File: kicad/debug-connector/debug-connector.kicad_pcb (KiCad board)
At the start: 2 copper layers, 4 parts, among them P1 CONN_02X10, P2 CONN_02X05, P3 CONN_01X04, P4 CONN_02X05

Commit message: Add outline and ground planes
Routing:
- net /TRST: track 38.1 -> 33.4 mm
- added copper zone on B.Cu, net GND
- added copper zone on F.Cu, net GND
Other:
- board outline added: 14.7 x 32.8 mm
- board text added: "GND"
- board text added: "RX"
- board text added: "TX"

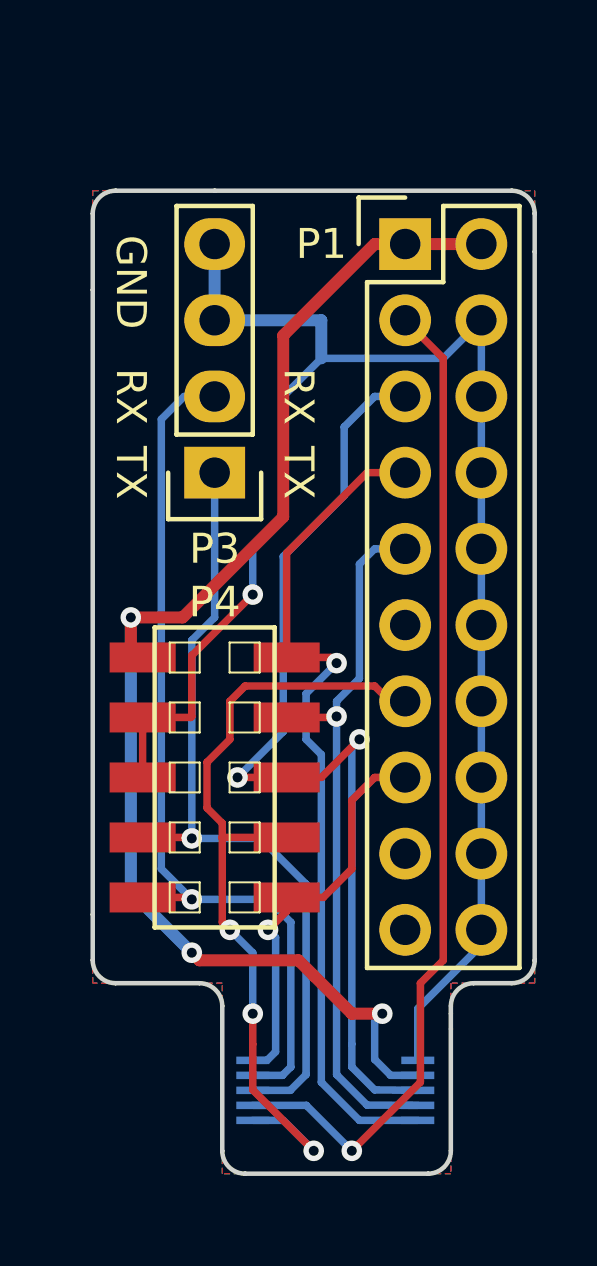
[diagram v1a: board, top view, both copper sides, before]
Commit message: Move debug connector to right and add text and logos on silkscreen.
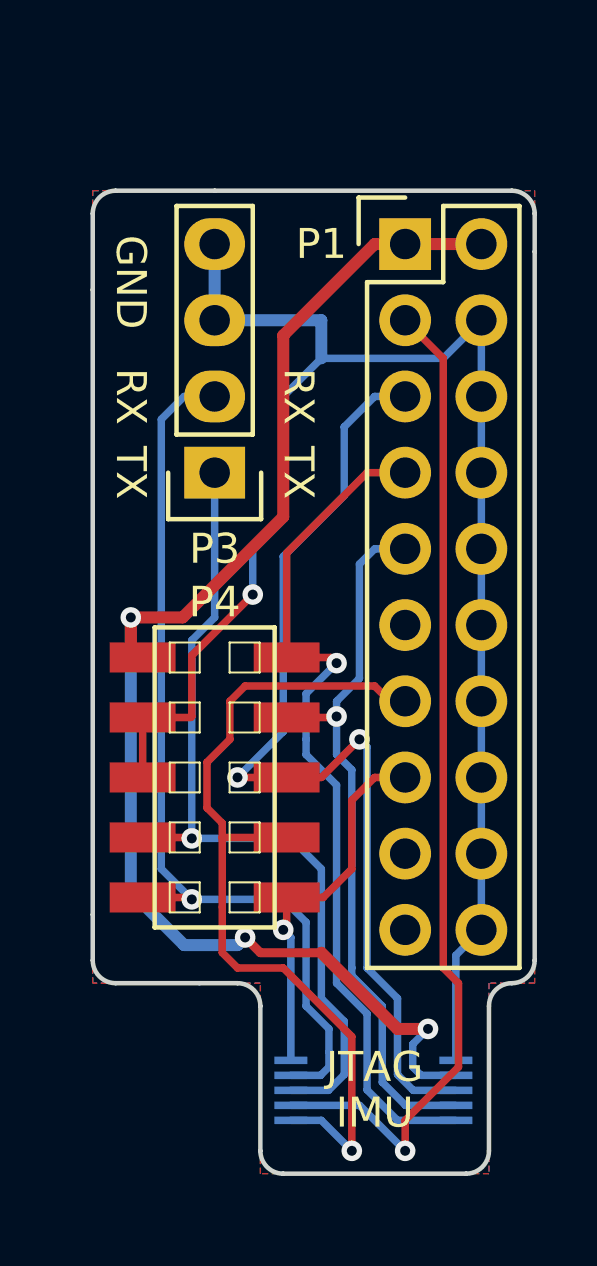
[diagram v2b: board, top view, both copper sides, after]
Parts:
- added G***: LOGO, logos:IMU_Logo_6x3mm, B.Cu at (162.3, 123.2)
- moved P2 1.27 mm to (162.6, 132.1)
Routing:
- net /VAPP: track 44.4 -> 46.1 mm
- net /TDO_SWO: track 28.4 -> 29.8 mm, vias 3 -> 1
- net /UART_TX: track 26.9 -> 28.1 mm
- net /NRST: track 13.6 -> 12.7 mm
- net /UART_RX: track 30.0 -> 30.8 mm
- net /TCK_SWCLK: track 23.9 -> 24.4 mm
- net /TMS_SWDIO: track 28.6 -> 29.2 mm
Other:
- outline, holes or cut-outs redrawn
- board text added: "IMU"
- board text added: "JTAG"
- board text added: "Jonas A 2015"
- board text added: "Rev A"

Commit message: Debug connector remade to better fit on IMU board.
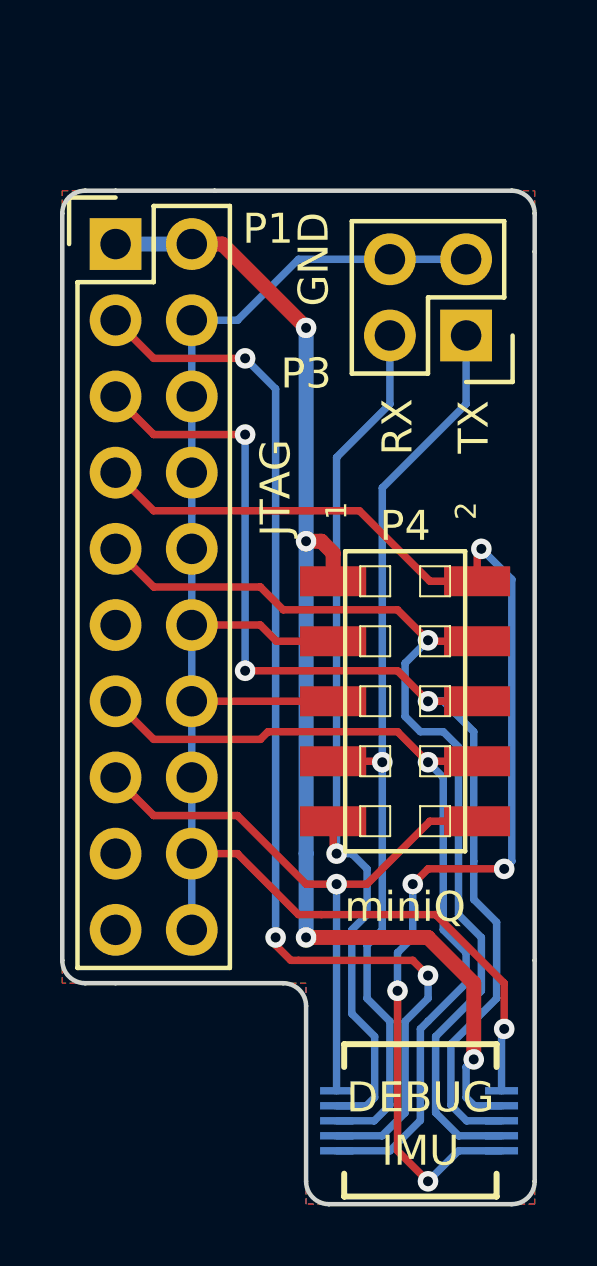
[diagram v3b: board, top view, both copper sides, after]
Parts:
- P3: footprint Pin_Headers:Pin_Header_Straight_1x04 -> Pin_Headers:Pin_Header_Straight_2x02
- moved G*** 12.9 mm to (165.9, 110.7), turned to 270 degrees
- moved P1 9.65 mm to (156.7, 102.9)
- moved P3 9.55 mm to (168.4, 105.9)
- moved P4 6.84 mm to (166.4, 118.1)
- moved P2 1.83 mm to (164.1, 133.1)
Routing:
- net /TMS_SWDIO: track 29.2 -> 42.6 mm, vias 1 -> 5
- net /TCK_SWCLK: track 24.4 -> 34.0 mm
- net /NRST: track 12.7 -> 21.3 mm
- net /VAPP: track 46.1 -> 41.3 mm, vias 3 -> 4
- net /TRST: track 33.6 -> 37.8 mm, vias 1 -> 3
- net /TDI: track 34.1 -> 38.1 mm, vias 2 -> 3
- net /UART_TX: track 28.1 -> 31.0 mm
- net /UART_RX: track 30.8 -> 29.9 mm
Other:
- board size 14.7 x 32.8 mm -> 15.7 x 33.8 mm
- board text added: "1"
- board text added: "2"
- board text added: "DEBUG"
- board text added: "miniQ"
